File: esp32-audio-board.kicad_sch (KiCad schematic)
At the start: 125 parts, among them IC1 LP2985A-33DBVR, J1 EN_PAD0, J10 PWR_LED+, J11 HP_LOUT1, J12 HP_ROUT1, J13 HP_LOUT2, J14 HP_ROUT2, J15 MIC_LIN1, J16 MIC_LIN1_GND, J17 MIC_RIN1, J18 MIC_RIN1_GND, J19 HP_GND1, J2 JST S2B, J20 HP_GND2, J21 VP_PAD0, J22 PWR_LED-, J23 CHG_LED+, J24 CHG_LED-, J3 USB_C_Receptacle_USB2.0_16P, J4 EN_PAD1, J5 VP_PAD1, J6 VN_PAD0, J7 VN_PAD1, J8 IO34_PAD0, J9 IO34_PAD1, Q1 SS8050, Q2 SS8050, Q4 AO3401A, U1 ESP32-WROOM-32E, U2 CP2102, U3 MCP73831-2-OT, U5 ES8388

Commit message: esp32-audio-board: refactor PCB
Added many changes to the PCB, which hopefully
will protect the PCB from EMI even better and
will ensure that all signals have a short return
path to GND plane. Added pads for a boot button
to allow the board to be flashed even if the
auto-download circuit will not work.

Signed-off-by: RaresCon <rares.constantin2002@gmail.com>
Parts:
- added BT_0: BOOT_PAD0, Connector_Wire:SolderWirePad_1x01_SMD_1x2mm, symbol Connector:Conn_01x01_Pin
- added BT_1: BOOT_PAD1, Connector_Wire:SolderWirePad_1x01_SMD_1x2mm, symbol Connector:Conn_01x01_Pin
- added C46: 0.1uF/10%, Capacitor_SMD:C_0402_1005Metric_Pad0.74x0.62mm_HandSolder, symbol Device:C
- C_EN1: value 1uF/10% -> 0.1uF/10%
- J21: value VP_PAD0 -> IO32_PAD0
- J5: value VP_PAD1 -> IO32_PAD1
- J6: value VN_PAD0 -> IO33_PAD0
- J7: value VN_PAD1 -> IO33_PAD1
- J8: value IO34_PAD0 -> IO25_PAD0
- J9: value IO34_PAD1 -> IO25_PAD1
- renumbered J1 to EN_0, J4 to EN_1, J19 to HP_G1, J20 to HP_G2, J11 to HP_L1, J13 to HP_L2, J12 to HP_R1, J14 to HP_R2, J15 to MI_L1, J16 to MI_LG1, J17 to MI_R1, J18 to MI_RG1
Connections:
- net ESP-IO0: now also BT_1.1 (Pin_1), C46.1
- net GND: now also BT_0.1 (Pin_1), C46.2
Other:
- note added: "BOOT"
- moved on the sheet: C15, C16, C17, C18, EN_0, EN_1, J21, J5, J6, J7, J8, J9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

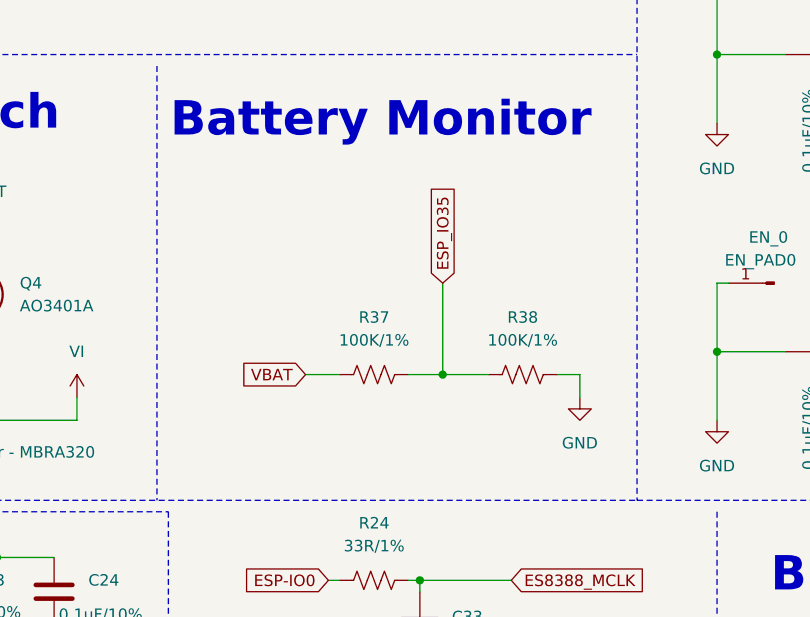
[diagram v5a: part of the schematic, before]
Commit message: esp32-audio-board: add bigger pads for pins
Added two new pads for audio pins and button pins
to allow larger cables to be soldered to the board.

Signed-off-by: RaresCon <rares.constantin2002@gmail.com>
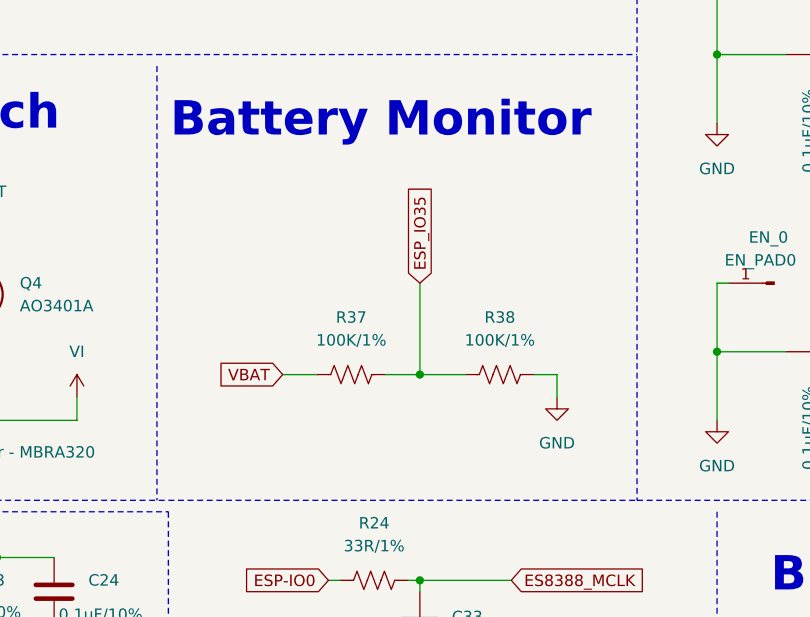
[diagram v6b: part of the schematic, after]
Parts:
- BT_0, BT_1, EN_0, EN_1, J10, J21, J22, J23, J24, J5, J6, J7, J8, J9: footprint Connector_Wire:SolderWirePad_1x01_SMD_1x2mm -> solderpads:SolderPad_SMD_2x2mm
- HP_G1, HP_G2, HP_L1, HP_L2, HP_R1, HP_R2, MI_L1, MI_LG1, MI_R1, MI_RG1: footprint Connector_Wire:SolderWirePad_1x01_SMD_1x2mm -> solderpads:SolderPad_SMD_2x3mm
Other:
- moved on the sheet: R37, R38
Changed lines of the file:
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@@
 	)
 	(junction
-		(at 269.24 120.65)
+		(at 266.7 120.65)
 		(diameter 0)
 		(color 0 0 0 0)
@@
 	(wire
 		(pts
-			(xy 284.48 120.65) (xy 284.48 123.19)
+			(xy 281.94 120.65) (xy 281.94 123.19)
 		)
 		(stroke
@@
 	(wire
 		(pts
-			(xy 254 120.65) (xy 257.81 120.65)
+			(xy 251.46 120.65) (xy 255.27 120.65)
 		)
 		(stroke
@@
 	(wire
 		(pts
-			(xy 281.94 120.65) (xy 284.48 120.65)
+			(xy 279.4 120.65) (xy 281.94 120.65)
 		)
 		(stroke
@@
 	(wire
 		(pts
-			(xy 265.43 120.65) (xy 269.24 120.65)
+			(xy 262.89 120.65) (xy 266.7 120.65)
 		)
 		(stroke
@@
 	(wire
 		(pts
-			(xy 269.24 110.49) (xy 269.24 120.65)
+			(xy 266.7 110.49) (xy 266.7 120.65)
 		)
 		(stroke
@@
 	(wire
 		(pts
-			(xy 269.24 120.65) (xy 274.32 120.65)
+			(xy 266.7 120.65) (xy 271.78 120.65)
 		)
 		(stroke
@@
 	(global_label "VBAT"
 		(shape input)
-		(at 254 120.65 180)
+		(at 251.46 120.65 180)
 		(fields_autoplaced yes)
 		(effects
@@
 		)
 		(property "Intersheetrefs" "${INTERSHEET_REFS}"
-			(at 246.6 120.65 0)
+			(at 244.06 120.65 0)
 			(effects
 				(font
@@
 	(global_label "ESP_IO35"
 		(shape input)
-		(at 269.24 110.49 90)
+		(at 266.7 110.49 90)
 		(fields_autoplaced yes)
 		(effects
@@
 		)
 		(property "Intersheetrefs" "${INTERSHEET_REFS}"
-			(at 269.24 98.5544 90)
+			(at 266.7 98.5544 90)
 			(effects
 				(font
@@
 			)
 		)
-		(property "Footprint" "Connector_Wire:SolderWirePad_1x01_SMD_1x2mm"
+		(property "Footprint" "solderpads:SolderPad_SMD_2x2mm"
 			(at 314.96 77.47 0)
 			(effects
@@
 			)
 		)
-		(property "Footprint" "Connector_Wire:SolderWirePad_1x01_SMD_1x2mm"
+		(property "Footprint" "solderpads:SolderPad_SMD_2x2mm"
 			(at 314.96 110.49 0)
 			(effects
@@
 			)
 		)
-		(property "Footprint" "Connector_Wire:SolderWirePad_1x01_SMD_1x2mm"
+		(property "Footprint" "solderpads:SolderPad_SMD_2x3mm"
 			(at 91.44 171.45 0)
 			(effects
@@
 			)
 		)
-		(property "Footprint" "Connector_Wire:SolderWirePad_1x01_SMD_1x2mm"
+		(property "Footprint" "solderpads:SolderPad_SMD_2x3mm"
 			(at 91.44 182.88 0)
 			(effects
@@
 			)
 		)
-		(property "Footprint" "Connector_Wire:SolderWirePad_1x01_SMD_1x2mm"
+		(property "Footprint" "solderpads:SolderPad_SMD_2x3mm"
 			(at 170.18 171.45 0)
 			(effects
@@
 	(symbol
 		(lib_id "power:GND")
-		(at 284.48 123.19 0)
+		(at 281.94 123.19 0)
 		(unit 1)
 		(exclude_from_sim no)
@@
 		(fields_autoplaced yes)
 		(property "Reference" "#PWR8"
-			(at 284.48 129.54 0)
+			(at 281.94 129.54 0)
 			(effects
 				(font
@@
 		)
 		(property "Value" "GND"
-			(at 284.48 128.27 0)
+			(at 281.94 128.27 0)
 			(effects
 				(font
@@
 		)
 		(property "Footprint" ""
-			(at 284.48 123.19 0)
+			(at 281.94 123.19 0)
 			(effects
 				(font
@@
 		)
 		(property "Datasheet" ""
-			(at 284.48 123.19 0)
+			(at 281.94 123.19 0)
 			(effects
 				(font
@@
 		)
 		(property "Description" "Power symbol creates a global label with name \"GND\" , ground"
-			(at 284.48 123.19 0)
+			(at 281.94 123.19 0)
 			(effects
 				(font
@@
 			)
 		)
-		(property "Footprint" "Connector_Wire:SolderWirePad_1x01_SMD_1x2mm"
+		(property "Footprint" "solderpads:SolderPad_SMD_2x3mm"
 			(at 170.18 182.88 0)
 			(effects
@@
 			)
 		)
-		(property "Footprint" "Connector_Wire:SolderWirePad_1x01_SMD_1x2mm"
+		(property "Footprint" "solderpads:SolderPad_SMD_2x2mm"
 			(at 275.59 27.94 0)
 			(effects
@@
 			)
 		)
-		(property "Footprint" "Connector_Wire:SolderWirePad_1x01_SMD_1x2mm"
+		(property "Footprint" "solderpads:SolderPad_SMD_2x3mm"
 			(at 278.13 269.24 0)
 			(effects
@@
 			)
 		)
-		(property "Footprint" "Connector_Wire:SolderWirePad_1x01_SMD_1x2mm"
+		(property "Footprint" "solderpads:SolderPad_SMD_2x2mm"
 			(at 353.06 152.4 0)
 			(effects
@@
 			)
 		)
-		(property "Footprint" "Connector_Wire:SolderWirePad_1x01_SMD_1x2mm"
+		(property "Footprint" "solderpads:SolderPad_SMD_2x2mm"
 			(at 361.95 226.06 0)
 			(effects
@@
 			)
 		)
-		(property "Footprint" "Connector_Wire:SolderWirePad_1x01_SMD_1x2mm"
+		(property "Footprint" "solderpads:SolderPad_SMD_2x2mm"
 			(at 306.07 77.47 0)
 			(effects
@@
 			)
 		)
-		(property "Footprint" "Connector_Wire:SolderWirePad_1x01_SMD_1x2mm"
+		(property "Footprint" "solderpads:SolderPad_SMD_2x2mm"
 			(at 353.06 189.23 0)
 			(effects
@@
 			)
 		)
-		(property "Footprint" "Connector_Wire:SolderWirePad_1x01_SMD_1x2mm"
+		(property "Footprint" "solderpads:SolderPad_SMD_2x3mm"
 			(at 278.13 273.05 0)
 			(effects
@@
 			)
 		)
-		(property "Footprint" "Connector_Wire:SolderWirePad_1x01_SMD_1x2mm"
+		(property "Footprint" "solderpads:SolderPad_SMD_2x2mm"
 			(at 90.17 129.54 0)
 			(effects
@@
 			)
 		)
-		(property "Footprint" "Connector_Wire:SolderWirePad_1x01_SMD_1x2mm"
+		(property "Footprint" "solderpads:SolderPad_SMD_2x2mm"
 			(at 353.06 226.06 0)
 			(effects
@@
 			)
 		)
-		(property "Footprint" "Connector_Wire:SolderWirePad_1x01_SMD_1x2mm"
+		(property "Footprint" "solderpads:SolderPad_SMD_2x2mm"
 			(at 361.95 189.23 0)
 			(effects
@@
 			)
 		)
-		(property "Footprint" "Connector_Wire:SolderWirePad_1x01_SMD_1x2mm"
+		(property "Footprint" "solderpads:SolderPad_SMD_2x2mm"
 			(at 361.95 152.4 0)
 			(effects
@@
 			)
 		)
-		(property "Footprint" "Connector_Wire:SolderWirePad_1x01_SMD_1x2mm"
+		(property "Footprint" "solderpads:SolderPad_SMD_2x3mm"
 			(at 278.13 232.41 0)
 			(effects
@@
 			)
 		)
-		(property "Footprint" "Connector_Wire:SolderWirePad_1x01_SMD_1x2mm"
+		(property "Footprint" "solderpads:SolderPad_SMD_2x2mm"
 			(at 273.05 27.94 0)
 			(effects
@@
 			)
 		)
-		(property "Footprint" "Connector_Wire:SolderWirePad_1x01_SMD_1x2mm"
+		(property "Footprint" "solderpads:SolderPad_SMD_2x3mm"
 			(at 170.18 191.77 0)
 			(effects
@@
 			)
 		)
-		(property "Footprint" "Connector_Wire:SolderWirePad_1x01_SMD_1x2mm"
+		(property "Footprint" "solderpads:SolderPad_SMD_2x2mm"
 			(at 90.17 127 0)
 			(effects
@@
 			)
 		)
-		(property "Footprint" "Connector_Wire:SolderWirePad_1x01_SMD_1x2mm"
+		(property "Footprint" "solderpads:SolderPad_SMD_2x3mm"
 			(at 91.44 191.77 0)
 			(effects
@@
 			)
 		)
-		(property "Footprint" "Connector_Wire:SolderWirePad_1x01_SMD_1x2mm"
+		(property "Footprint" "solderpads:SolderPad_SMD_2x2mm"
 			(at 306.07 110.49 0)
 			(effects
@@
 	(symbol
 		(lib_id "Device:R_US")
-		(at 278.13 120.65 90)
+		(at 275.59 120.65 90)
 		(unit 1)
 		(exclude_from_sim no)
@@
 		(fields_autoplaced yes)
 		(property "Reference" "R38"
-			(at 278.13 114.3 90)
+			(at 275.59 114.3 90)
 			(effects
 				(font
@@
 		)
 		(property "Value" "100K/1%"
-			(at 278.13 116.84 90)
+			(at 275.59 116.84 90)
 			(effects
 				(font
@@
 		)
 		(property "Footprint" "Resistor_SMD:R_0402_1005Metric_Pad0.72x0.64mm_HandSolder"
-			(at 278.384 119.634 90)
+			(at 275.844 119.634 90)
 			(effects
 				(font
@@
 		)
 		(property "Datasheet" "~"
-			(at 278.13 120.65 0)
+			(at 275.59 120.65 0)
 			(effects
 				(font
@@
 		)
 		(property "Description" "Resistor, US symbol"
-			(at 278.13 120.65 0)
+			(at 275.59 120.65 0)
 			(effects
 				(font
@@
 		)
 		(property "Arrow Part Number" ""
-			(at 278.13 120.65 0)
+			(at 275.59 120.65 0)
 			(effects
 				(font
@@
 		)
 		(property "Arrow Price/Stock" ""
-			(at 278.13 120.65 0)
+			(at 275.59 120.65 0)
 			(effects
 				(font
@@
 	(symbol
 		(lib_id "Device:R_US")
-		(at 261.62 120.65 90)
+		(at 259.08 120.65 90)
 		(unit 1)
 		(exclude_from_sim no)
@@
 		(fields_autoplaced yes)
 		(property "Reference" "R37"
-			(at 261.62 114.3 90)
+			(at 259.08 114.3 90)
 			(effects
 				(font
@@
 		)
 		(property "Value" "100K/1%"
-			(at 261.62 116.84 90)
+			(at 259.08 116.84 90)
 			(effects
 				(font
@@
 		)
 		(property "Footprint" "Resistor_SMD:R_0402_1005Metric_Pad0.72x0.64mm_HandSolder"
-			(at 261.874 119.634 90)
+			(at 259.334 119.634 90)
 			(effects
 				(font
@@
 		)
 		(property "Datasheet" "~"
-			(at 261.62 120.65 0)
+			(at 259.08 120.65 0)
 			(effects
 				(font
@@
 		)
 		(property "Description" "Resistor, US symbol"
-			(at 261.62 120.65 0)
+			(at 259.08 120.65 0)
 			(effects
 				(font
@@
 		)
 		(property "Arrow Part Number" ""
-			(at 261.62 120.65 0)
+			(at 259.08 120.65 0)
 			(effects
 				(font
@@
 		)
 		(property "Arrow Price/Stock" ""
-			(at 261.62 120.65 0)
+			(at 259.08 120.65 0)
 			(effects
 				(font
@@
 			)
 		)
-		(property "Footprint" "Connector_Wire:SolderWirePad_1x01_SMD_1x2mm"
+		(property "Footprint" "solderpads:SolderPad_SMD_2x3mm"
 			(at 278.13 228.6 0)
 			(effects

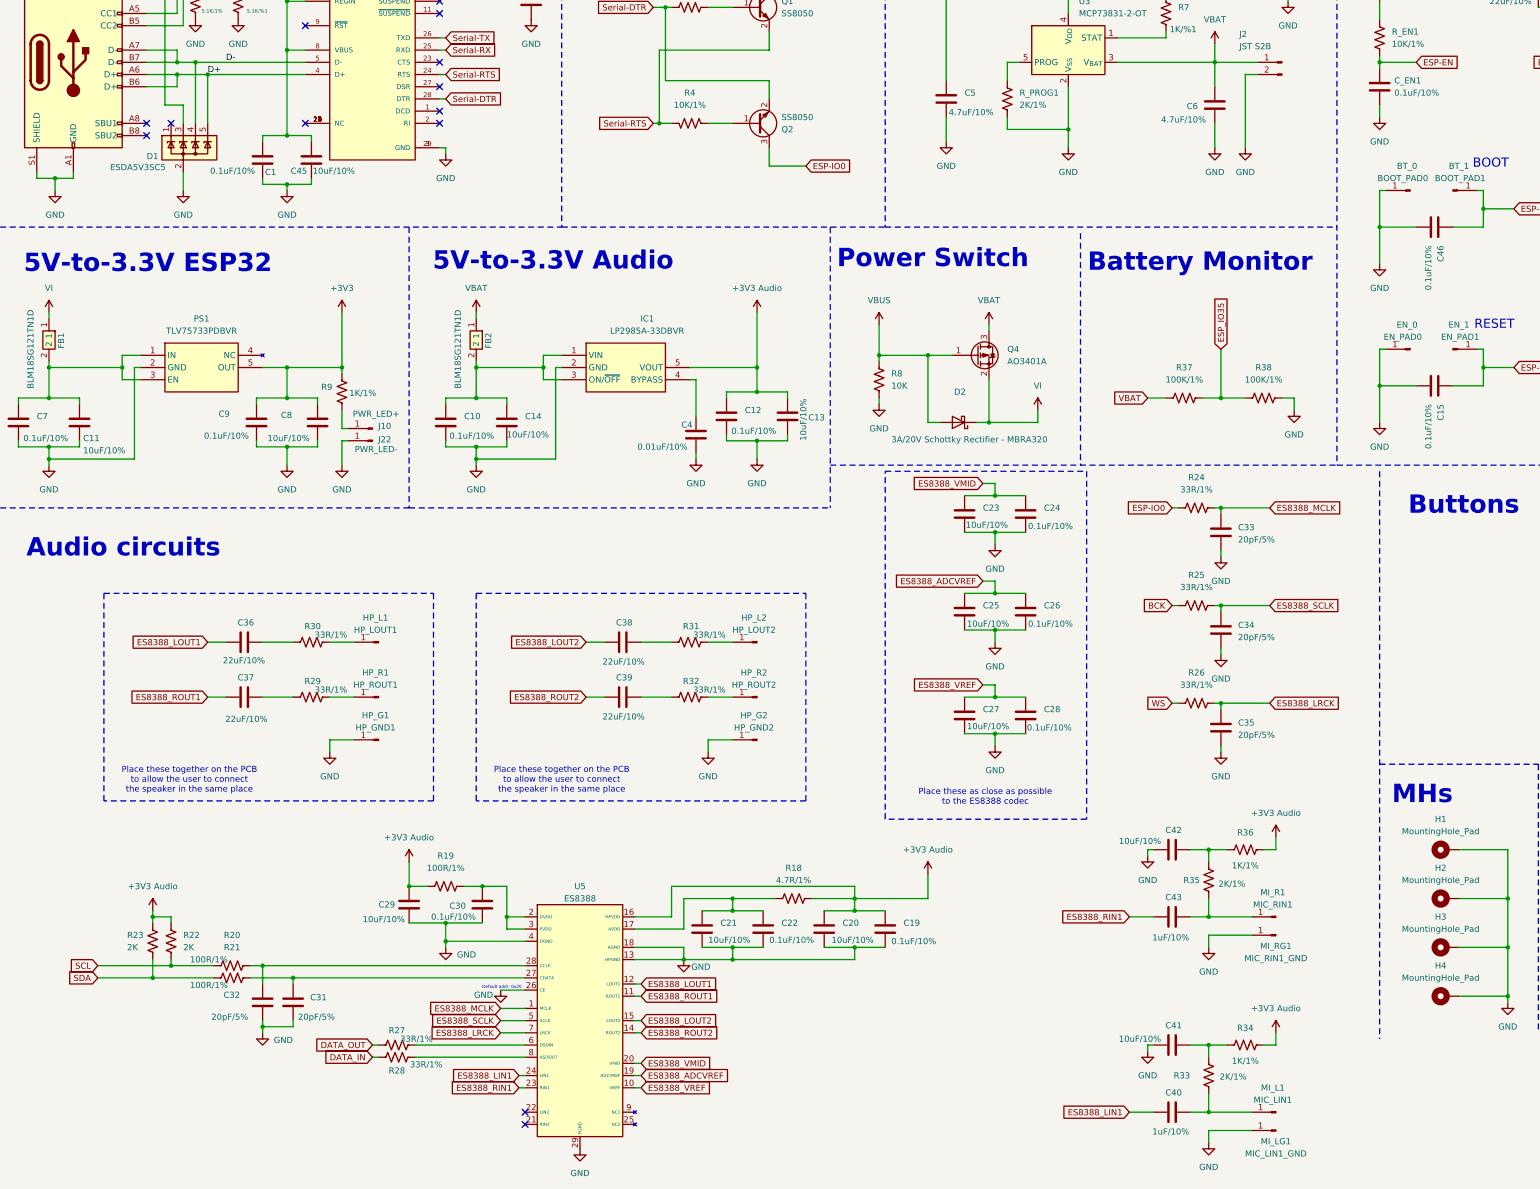
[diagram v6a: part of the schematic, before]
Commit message: esp32-audio-board: add testpoints and tweaks
Added testpoints for SDA/SCL lines to allow for
rising edge refinements if needed for ES8388.
Checked all the decoupling capacitors and viases
for mistakes, fixed (hopefully) all of them.

Sent the board in production!

Signed-off-by: RaresCon <rares.constantin2002@gmail.com>
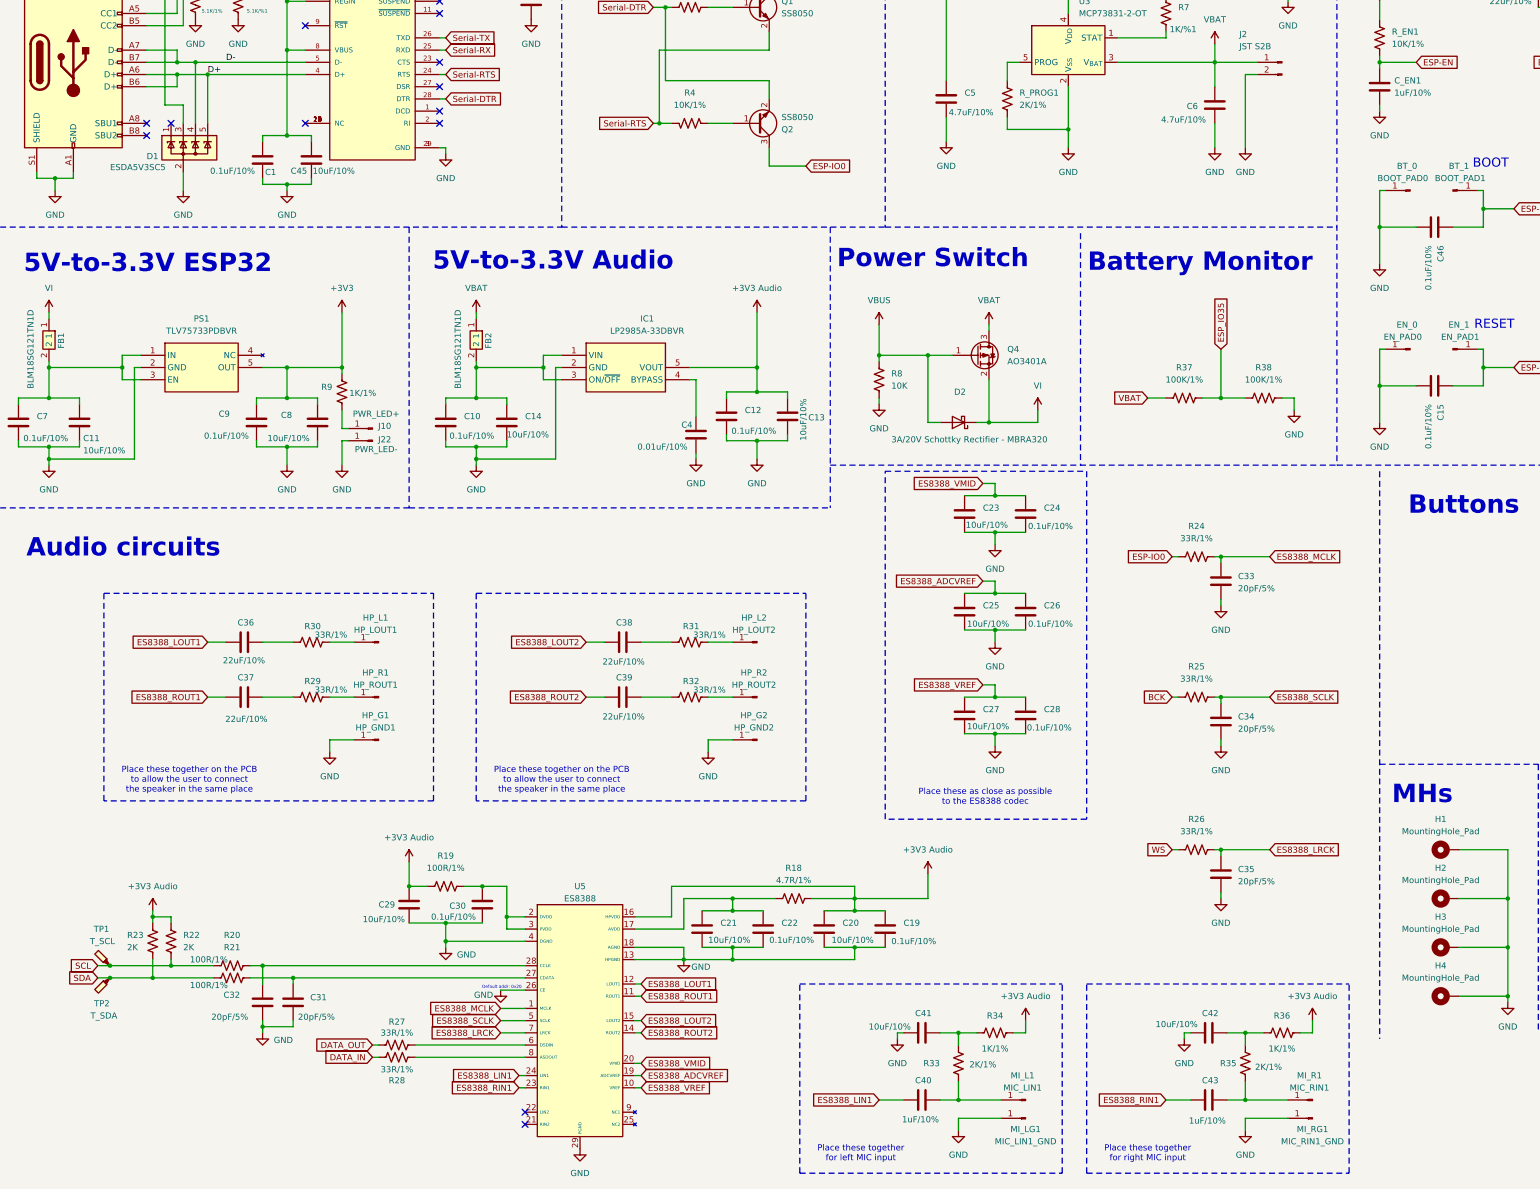
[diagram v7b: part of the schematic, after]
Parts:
- added TP1: T_SCL, TestPoint:TestPoint_Pad_D1.0mm, symbol Connector:TestPoint_Probe
- added TP2: T_SDA, TestPoint:TestPoint_Pad_D1.0mm, symbol Connector:TestPoint_Probe
- C_EN1: value 0.1uF/10% -> 1uF/10%
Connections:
- net SCL: now also TP1.1
- net SDA: now also TP2.1
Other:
- note added: "Place these together for left MIC input"
- note added: "Place these together for right MIC input"
- moved on the sheet: C33, C34, C35, C40, C41, C42, C43, MI_L1, MI_LG1, MI_R1, MI_RG1, R24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
